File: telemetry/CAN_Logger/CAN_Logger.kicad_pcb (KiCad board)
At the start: 2 copper layers, 109.3 x 58.3 mm, 59 parts, among them J1 CONN_02X03, J2 SD_socket, J3 MM_F_RA_20, U1 MCP2561-E_SN, U101 TPS560430YF, U2 ATMEGA16M1, U3 LM3480, U4 TXB0104, Y1 Crystal_SMD

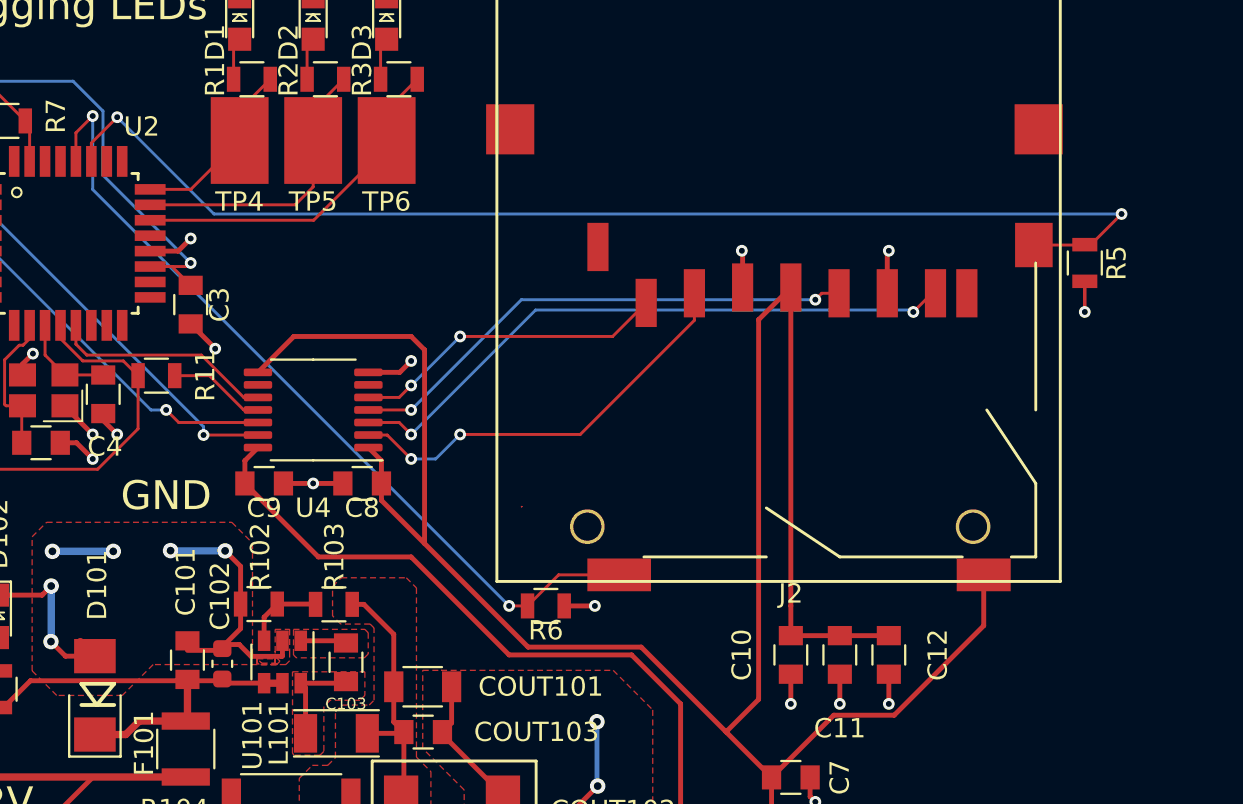
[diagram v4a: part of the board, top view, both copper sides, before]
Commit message: Fixed via wire for SD_Protect, edited labels
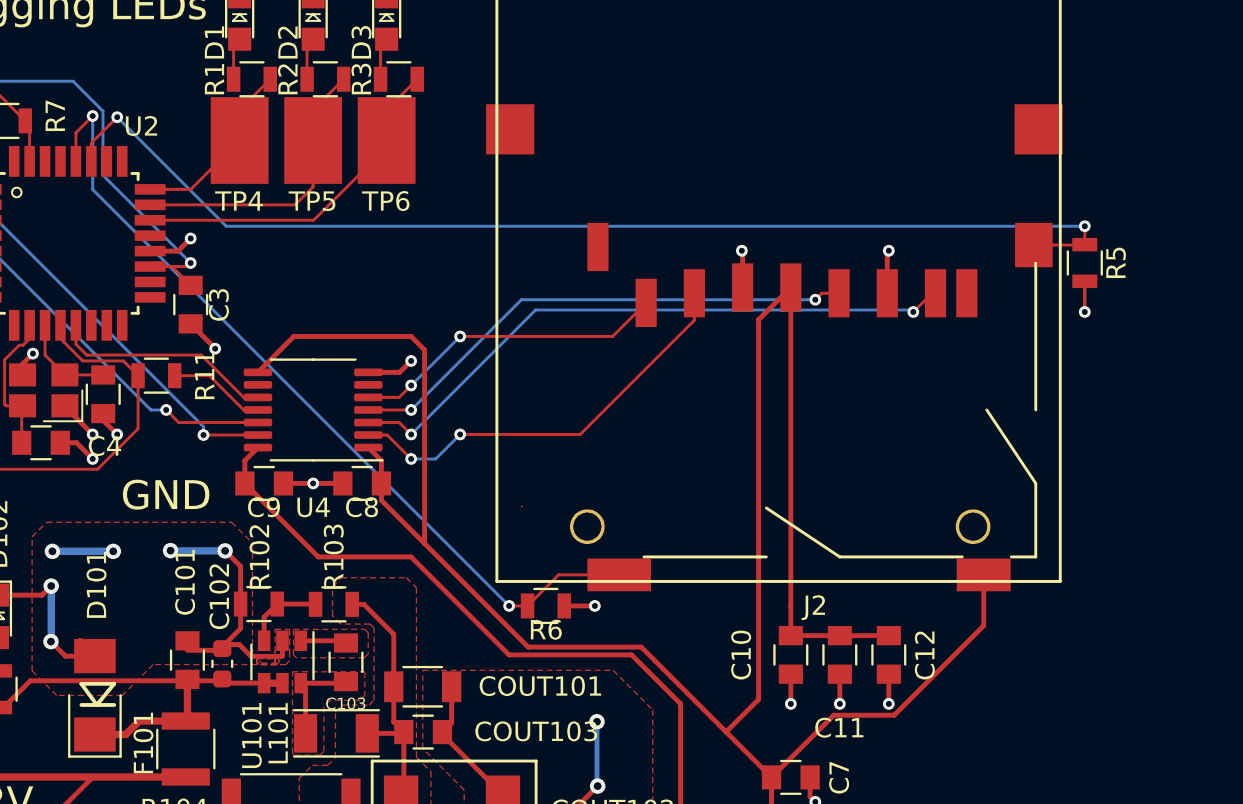
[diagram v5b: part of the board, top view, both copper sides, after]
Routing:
- net /SD_PROTECT: track 62.2 -> 59.3 mm

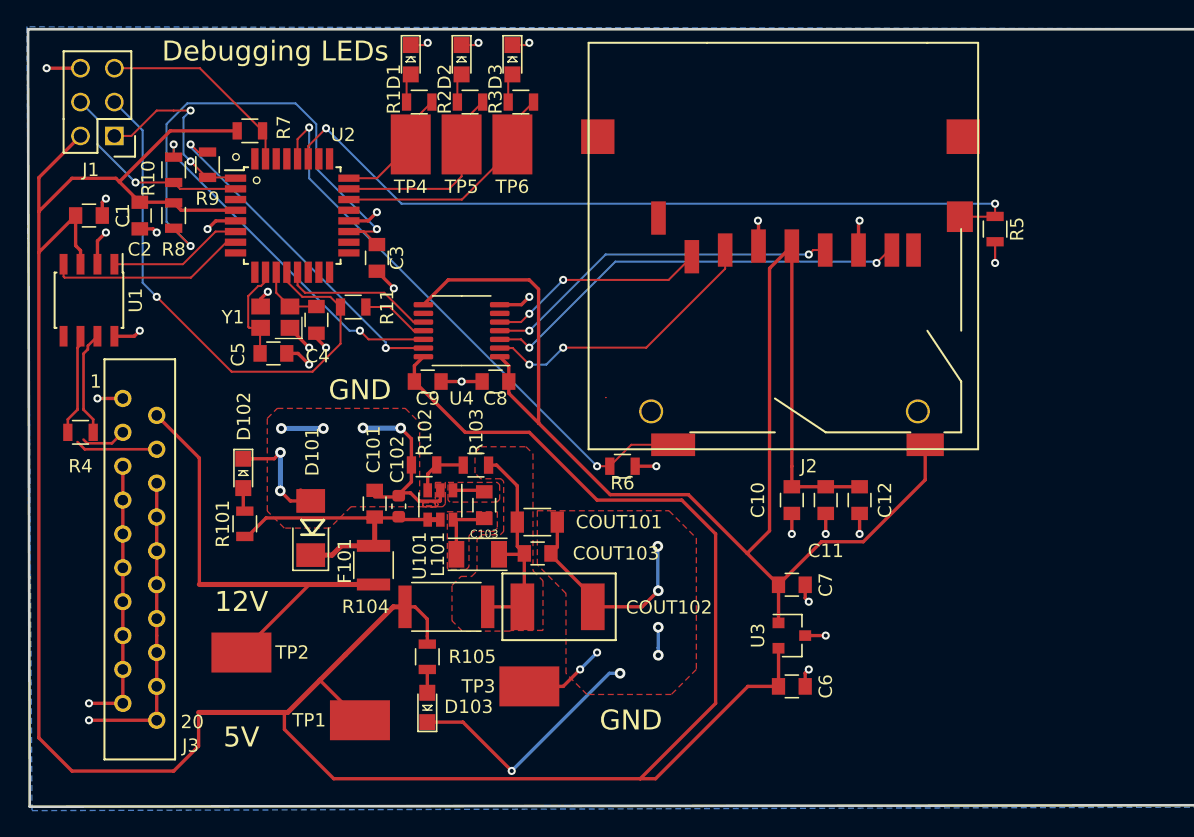
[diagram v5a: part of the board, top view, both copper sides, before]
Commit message: Rearranging layout, changed 3.3V to 3V3
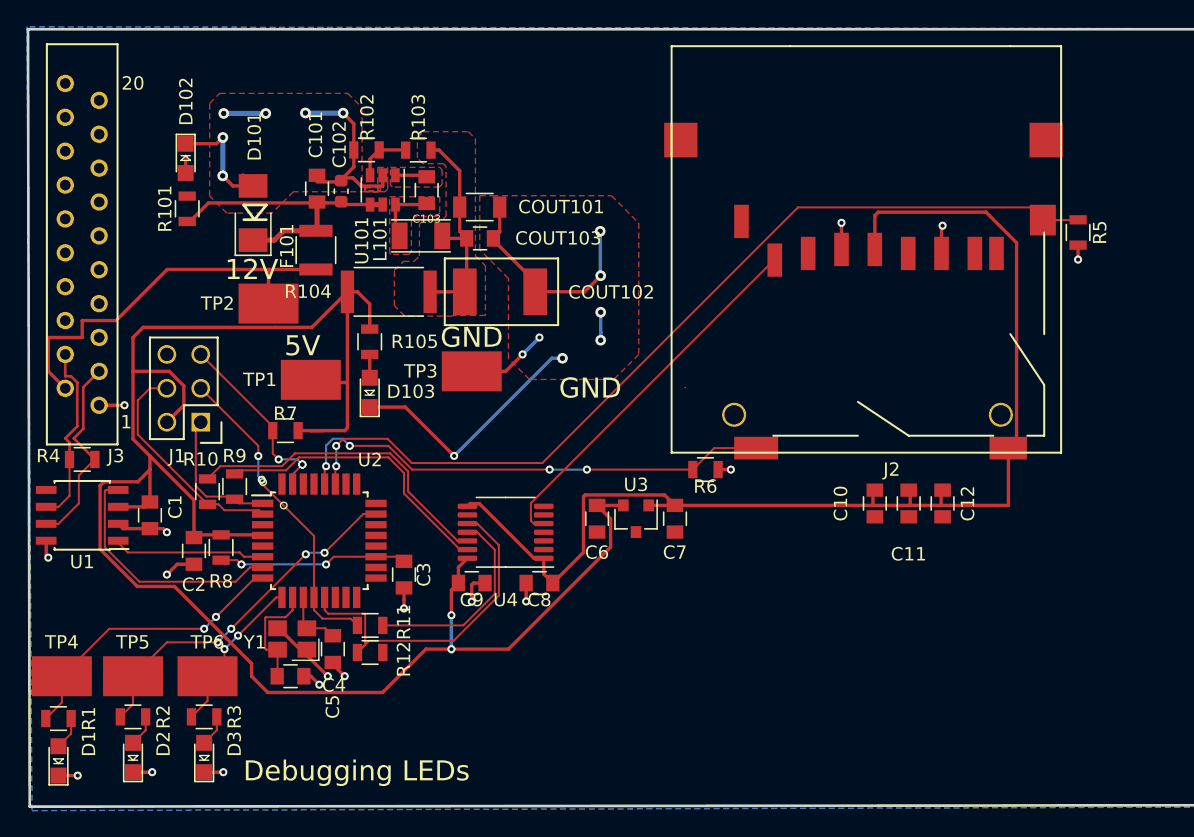
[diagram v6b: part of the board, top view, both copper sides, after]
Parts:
- added R12: R_10K, footprints:R_0805_OEM, F.Cu at (124.0, 123.2)
- moved D1 58.8 mm to (100.6, 131.3), turned to 90 degrees
- moved D2 57.8 mm to (106.2, 131.1), turned to 90 degrees
- moved D3 57.2 mm to (111.5, 131.1), turned to 90 degrees
- moved R1 53.6 mm to (100.6, 128.1), turned to 180 degrees
- moved R2 52.6 mm to (106.2, 128.0), turned to 180 degrees
- moved R3 51.9 mm to (111.5, 128.0), turned to 180 degrees
- moved TP4 47.7 mm to (100.8, 125.0), turned to 180 degrees
- moved TP5 46.9 mm to (106.2, 125.0), turned to 180 degrees
- moved TP6 46.0 mm to (111.8, 125.0), turned to 180 degrees
- moved TP2 26.2 mm to (116.3, 97.0)
- moved TP1 25.8 mm to (119.5, 102.7)
- moved C2 25.5 mm to (110.7, 115.6)
- moved R8 25.1 mm to (112.8, 115.3)
- moved C4 24.7 mm to (121.2, 122.9)
- moved U2 24.5 mm to (120.1, 114.8)
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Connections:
- net /CS_3.3V renamed /CS_3V3
- net /MISO_3.3V renamed /MISO_3V3
- net /MOSI_3.3V renamed /MOSI_3V3
- net /SCK_3.3V renamed /SCK_3V3
- U2 pad 22: /P_LED_3 -> Net-(U2-Pad22)
- U2 pad 24: /P_LED_1 -> Net-(U2-Pad24)
- U2 pad 8: Net-(U2-Pad8) -> /P_LED_1
- U2 pad 9: Net-(U2-Pad9) -> /P_LED_3
- U4 pad 10: /CS -> /CS_SD
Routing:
- net +5V: track 220.7 -> 146.0 mm, vias 0 -> 2
- net GND: track 167.8 -> 105.7 mm, vias 44 -> 31
- net /MOSI_3V3: track 32.8 -> 0.00 mm, vias 2 -> 0
- net +3V3: track 117.0 -> 89.1 mm
- net /SCK_3V3: track 26.9 -> 0.00 mm, vias 2 -> 0
- net /CS_SD: track 0.00 -> 26.4 mm
- net Net-(C3-Pad1): track 39.8 -> 14.7 mm
- net /MISO_3V3: track 21.8 -> 0.00 mm, vias 2 -> 0
- net /SCK: track 41.2 -> 23.9 mm, vias 1 -> 2
- net /P_LED_1: track 9.52 -> 22.0 mm, vias 0 -> 2
- net /CS_3V3: track 16.4 -> 28.2 mm, vias 2 -> 0
- net /P_LED_2: track 15.1 -> 26.7 mm, vias 0 -> 4
- net /CS: track 11.6 -> 0.00 mm
- net /SCK_SD: track 5.05 -> 15.3 mm
- net /SD_PROTECT: track 59.3 -> 67.8 mm
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
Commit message: Completed 2nd revision of PCB layout
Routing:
- net /MOSI_3V3: track 0.00 -> 43.2 mm
- net /SCK_3V3: track 0.00 -> 37.7 mm
- net /MISO_3V3: track 0.00 -> 35.2 mm
- net GND: track 105.7 -> 119.4 mm, vias 31 -> 40
- net +5V: track 146.0 -> 148.8 mm
- net /SCK_SD: track 15.3 -> 16.0 mm

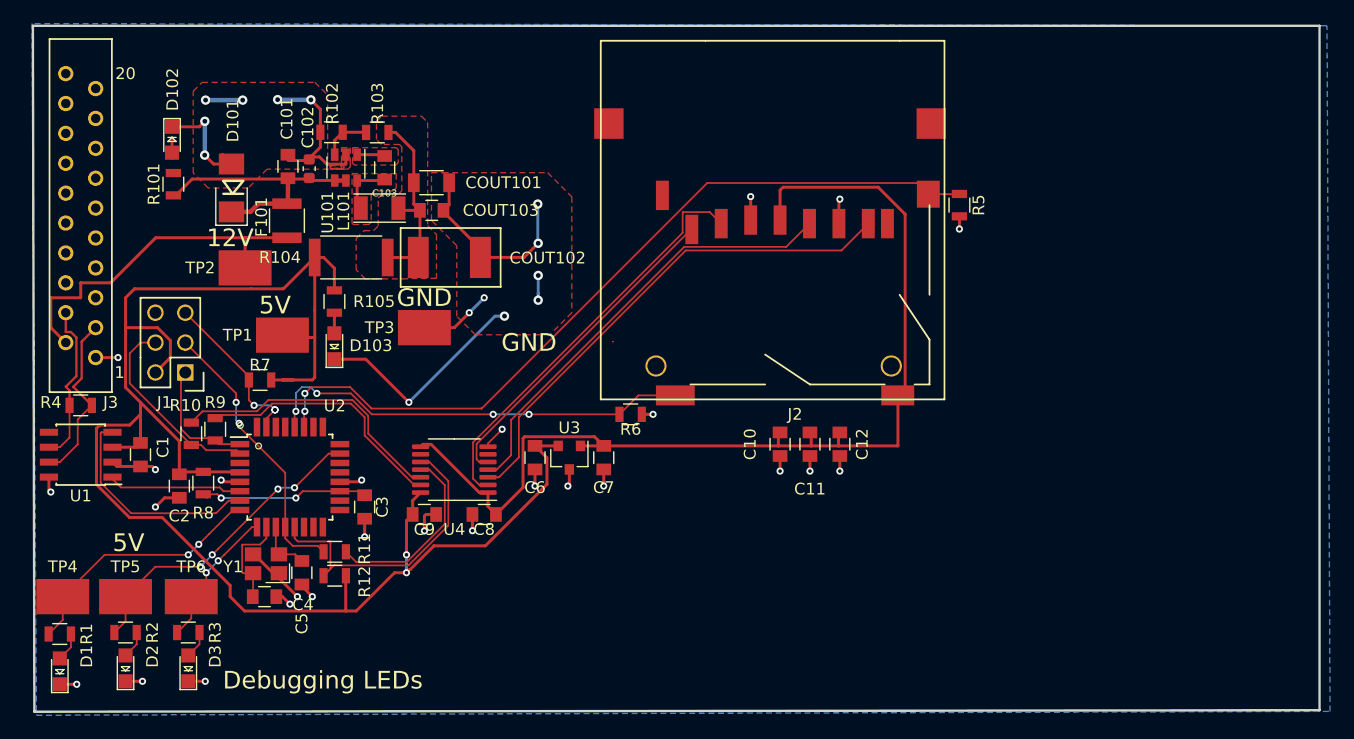
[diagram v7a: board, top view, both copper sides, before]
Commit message: Added curved edges and missing trace to PCB, moved connector to edge
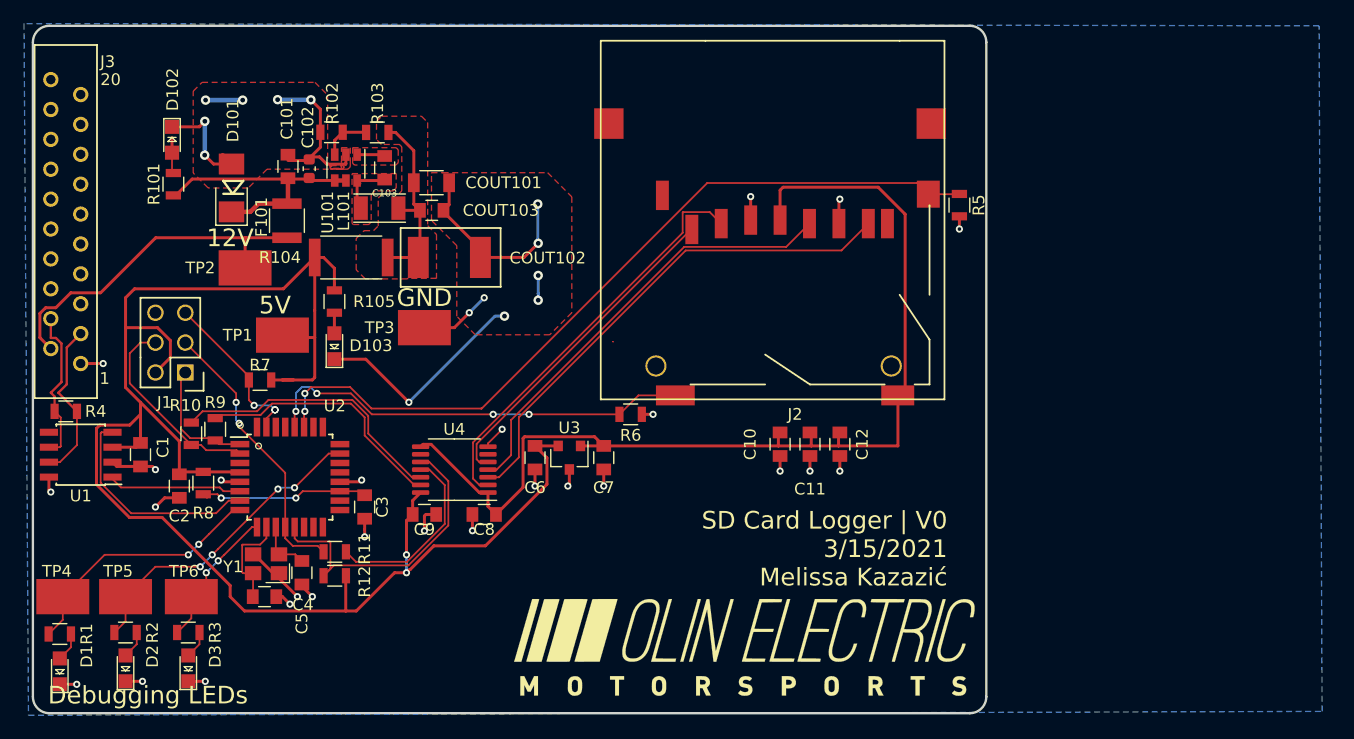
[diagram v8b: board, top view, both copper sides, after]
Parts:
- added G***: LOGO, footprints:Logo_Large, F.Cu at (158.8, 129.3)
- moved G*** 58.2 mm to (158.9, 129.4)
- moved G*** 51.3 mm to (128.3, 105.7)
- moved J3 1.37 mm to (102.4, 100.1)
- moved R4 1.37 mm to (101.1, 109.2)
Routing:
- net Net-(D102-Pad2): track 1.75 -> 3.53 mm
- net /CAN_P: track 14.9 -> 13.9 mm
- net /CAN_N: track 13.8 -> 13.2 mm
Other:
- board size 109.3 x 58.3 mm -> 81 x 58.4 mm
- board text added: "SD Card Logger | V0 3/15/2021 Melissa Kazazić"
